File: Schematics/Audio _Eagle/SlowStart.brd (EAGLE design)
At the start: 99.1 x 76.2 mm, 20 parts, among them P1 MOLEX_6P

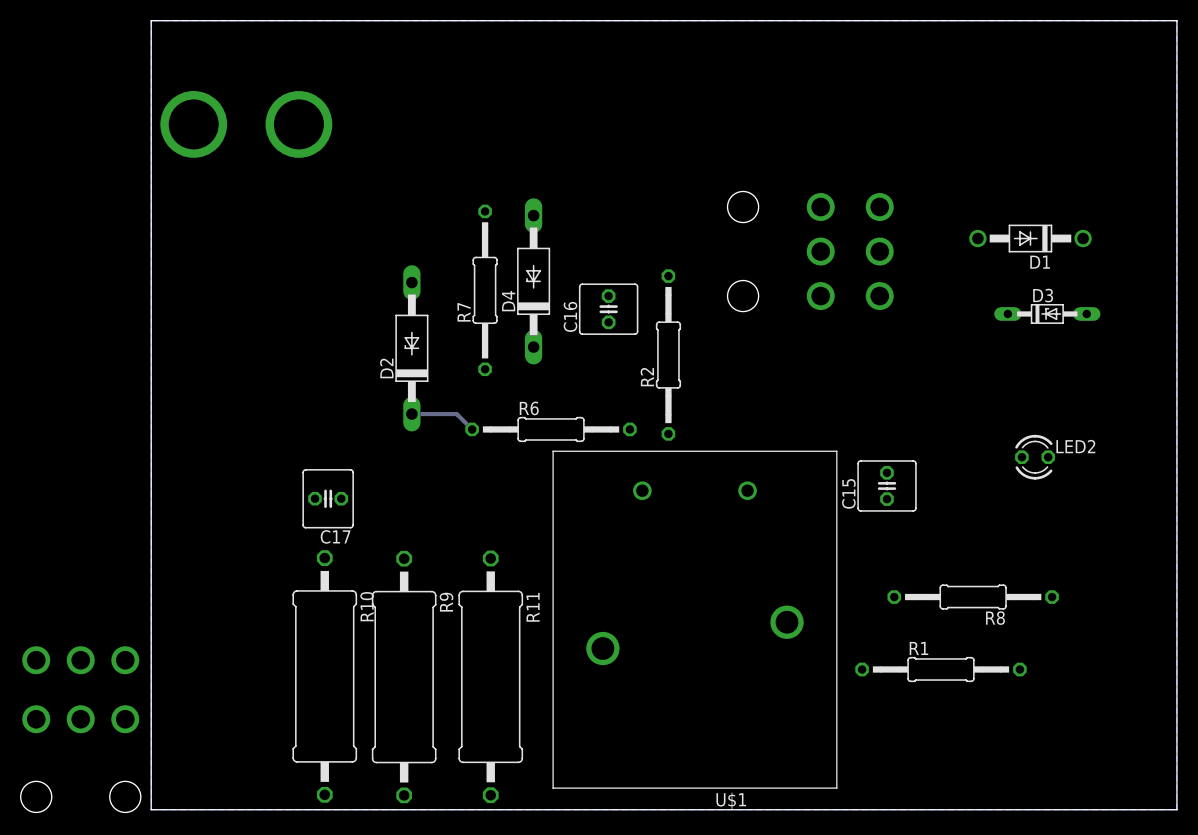
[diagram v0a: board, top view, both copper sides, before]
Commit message: created screw terminal and added data sheet
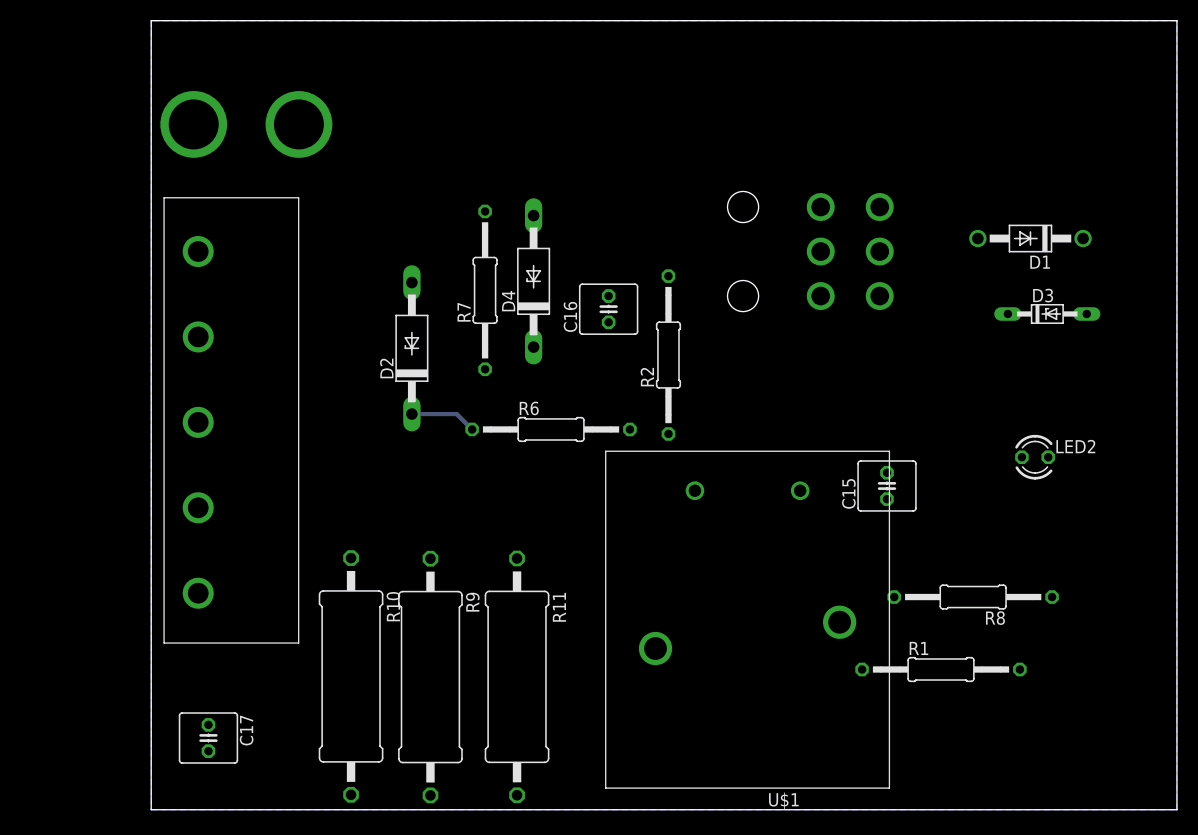
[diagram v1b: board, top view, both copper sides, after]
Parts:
- removed P1: MOLEX_6P, Amplifier_Parts:MOLEX_6P
- added U$2: SCREW_TERMINAL_5, Amplifier_Parts:SCREW_TERMINAL_5
- moved C17 25.8 mm to (5.53, 6.93), turned to 270 degrees
- moved U$1 5.08 mm to (57.6, 23.2)
- moved R10 2.54 mm to (19.3, 12.9)
- moved R11 2.54 mm to (35.3, 12.8)
- moved R9 2.54 mm to (27.0, 12.8)
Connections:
- removed net N$6: P1.P$6, U$4.P$2
- new net N$2: U$2.P$6, U$4.P$2
- net GND: now also U$2.P$5; no longer P1.P$4
- net N$1: now also U$2.P$2; no longer P1.P$1
- net VAC+: now also U$2.P$4; no longer P1.P$3
- net VAC-: now also U$2.P$3; no longer P1.P$2
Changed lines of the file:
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@@
 <element name="R7" library="resistor" package="0207/15" value="390" x="32.2445875" y="50.158621875" rot="R90"/>
 <element name="R8" library="resistor" package="0207/15" value="10k" x="79.379503125" y="20.540834375" rot="R180"/>
-<element name="R9" library="rcl" package="0617/22" value="68" x="24.427478125" y="12.812734375" rot="R270"/>
+<element name="R9" library="rcl" package="0617/22" value="68" x="26.967478125" y="12.812734375" rot="R270"/>
 <element name="C15" library="rcl" package="C025-060X050" value="1uF" x="71.058725" y="31.26728125" rot="R90"/>
 <element name="C16" library="rcl" package="C025-060X050" value="1uF" x="44.175" y="48.33925625" rot="R90"/>
-<element name="C17" library="rcl" package="C025-060X050" value="0.01uF" x="17.0871" y="30.03140625" rot="R180"/>
+<element name="C17" library="rcl" package="C025-060X050" value="0.01uF" x="5.52859375" y="6.9271" rot="R270"/>
 <element name="D1" library="diode" package="DO41-10" value="1N4004" x="84.913978125" y="55.1643875" rot="R180"/>
 <element name="D2" library="diode" package="P1Z12" value="22V" x="25.174603125" y="44.561271875" rot="R90"/>
 <element name="D3" library="diode" package="DO34Z7" value="3.9V" x="86.54215" y="47.877403125"/>
 <element name="D4" library="diode" package="P1Z12" value="28V" x="36.930628125" y="51.028159375" rot="R90"/>
-<element name="R10" library="rcl" package="0617/22" value="68" x="16.760721875" y="12.873171875" rot="R270"/>
-<element name="R11" library="rcl" package="0617/22" value="68" x="32.789928125" y="12.83155" rot="R270"/>
-<element name="U$1" library="Amplifier_Parts" package="RELAY_CM" value="T9AS1D" x="52.512303125" y="23.188921875" rot="R180"/>
+<element name="R10" library="rcl" package="0617/22" value="68" x="19.300721875" y="12.873171875" rot="R270"/>
+<element name="R11" library="rcl" package="0617/22" value="68" x="35.329928125" y="12.83155" rot="R270"/>
+<element name="U$1" library="Amplifier_Parts" package="RELAY_CM" value="T9AS1D" x="57.592303125" y="23.188921875" rot="R180"/>
 <element name="LED2" library="led" package="LED3MM" value="TLLG4400" x="85.359234375" y="34.044678125">
 <attribute name="MF" value="VISHAY SEMICONDUCTOR" x="122.189234375" y="-31.995321875" size="1.778" layer="27" display="off"/>
@@
 <element name="R2" library="resistor" package="0207/15" value="100" x="49.953821875" y="43.912103125" rot="R90"/>
 <element name="U$4" library="Amplifier_Parts" package="FUSE_PADS" value="FUSE" x="9.1866" y="66.183428125" rot="R180"/>
-<element name="P1" library="Amplifier_Parts" package="MOLEX_6P" value="MOLEX_6P" x="-8.9535" y="6.319090625"/>
+<element name="U$2" library="Amplifier_Parts" package="SCREW_TERMINAL_5" value="SCREW_TERMINAL_5" x="2.54" y="38.1" rot="R270"/>
 </elements>
 <signals>
@@
 <contactref element="LED2" pad="K"/>
 <contactref element="R2" pad="1"/>
-<contactref element="P1" pad="P$4"/>
 <polygon width="0.4064" layer="16" isolate="1.27">
 <vertex x="0" y="0"/>
@@
 <vertex x="0" y="76.2"/>
 </polygon>
-<wire x1="36.930628125" y1="57.378159375" x2="-11.1035" y2="14.439090625" width="0" layer="19" extent="1-1"/>
+<contactref element="U$2" pad="P$5"/>
 </signal>
 <signal name="VCC">
@@
 <contactref element="C17" pad="1"/>
 <contactref element="U$1" pad="COM"/>
-<contactref element="P1" pad="P$2"/>
-<wire x1="32.789928125" y1="24.26155" x2="61.402303125" y2="18.108921875" width="0" layer="19" extent="1-1"/>
-<wire x1="24.427478125" y1="24.242734375" x2="32.789928125" y2="24.26155" width="0" layer="19" extent="1-1"/>
-<wire x1="16.760721875" y1="24.303171875" x2="24.427478125" y2="24.242734375" width="0" layer="19" extent="1-1"/>
-<wire x1="18.3571" y1="30.03140625" x2="16.760721875" y2="24.303171875" width="0" layer="19" extent="1-1"/>
-<wire x1="-11.1035" y1="8.739090625" x2="16.760721875" y2="24.303171875" width="0" layer="19" extent="1-1"/>
+<contactref element="U$2" pad="P$3"/>
+<wire x1="35.329928125" y1="24.26155" x2="66.482303125" y2="18.108921875" width="0" layer="19" extent="1-1"/>
+<wire x1="26.967478125" y1="24.242734375" x2="35.329928125" y2="24.26155" width="0" layer="19" extent="1-1"/>
+<wire x1="19.300721875" y1="24.303171875" x2="26.967478125" y2="24.242734375" width="0" layer="19" extent="1-1"/>
+<wire x1="4.54" y1="37.41" x2="19.300721875" y2="24.303171875" width="0" layer="19" extent="1-1"/>
+<wire x1="5.52859375" y1="8.1971" x2="19.300721875" y2="24.303171875" width="0" layer="19" extent="1-1"/>
 </signal>
 <signal name="N$8">
@@
 <contactref element="C17" pad="2"/>
 <contactref element="U$1" pad="NO"/>
-<wire x1="43.622303125" y1="15.568921875" x2="70.35879375" y2="58.208578125" width="0" layer="19" extent="1-1"/>
-<wire x1="32.789928125" y1="1.40155" x2="43.622303125" y2="15.568921875" width="0" layer="19" extent="1-1"/>
-<wire x1="24.427478125" y1="1.382734375" x2="32.789928125" y2="1.40155" width="0" layer="19" extent="1-1"/>
-<wire x1="16.760721875" y1="1.443171875" x2="24.427478125" y2="1.382734375" width="0" layer="19" extent="1-1"/>
-<wire x1="15.8171" y1="30.03140625" x2="16.760721875" y2="1.443171875" width="0" layer="19" extent="1-1"/>
+<wire x1="48.702303125" y1="15.568921875" x2="70.35879375" y2="58.208578125" width="0" layer="19" extent="1-1"/>
+<wire x1="35.329928125" y1="1.40155" x2="48.702303125" y2="15.568921875" width="0" layer="19" extent="1-1"/>
+<wire x1="26.967478125" y1="1.382734375" x2="35.329928125" y2="1.40155" width="0" layer="19" extent="1-1"/>
+<wire x1="19.300721875" y1="1.443171875" x2="26.967478125" y2="1.382734375" width="0" layer="19" extent="1-1"/>
+<wire x1="5.52859375" y1="5.6571" x2="19.300721875" y2="1.443171875" width="0" layer="19" extent="1-1"/>
 </signal>
 <signal name="N$10">
@@
 <contactref element="C16" pad="1"/>
 <contactref element="U$1" pad="COIL-"/>
-<wire x1="44.175" y1="47.06925625" x2="89.993978125" y2="55.1643875" width="0" layer="19" extent="1-1"/>
+<wire x1="52.512303125" y1="30.808921875" x2="89.993978125" y2="55.1643875" width="0" layer="19" extent="1-1"/>
+<wire x1="44.175" y1="47.06925625" x2="52.512303125" y2="30.808921875" width="0" layer="19" extent="1-1"/>
 <wire x1="36.930628125" y1="44.678159375" x2="44.175" y2="47.06925625" width="0" layer="19" extent="1-1"/>
 <wire x1="32.2445875" y1="57.778621875" x2="36.930628125" y2="44.678159375" width="0" layer="19" extent="1-1"/>
-<wire x1="47.432303125" y1="30.808921875" x2="44.175" y2="47.06925625" width="0" layer="19" extent="1-1"/>
 </signal>
 <signal name="N$11">
@@
 <signal name="N$1">
 <contactref element="U$4" pad="P$1"/>
-<contactref element="P1" pad="P$1"/>
-<wire x1="-2.5035" y1="8.739090625" x2="14.2666" y2="66.183428125" width="0" layer="19" extent="1-1"/>
-</signal>
-<signal name="N$6">
-<contactref element="U$4" pad="P$2"/>
-<contactref element="P1" pad="P$6"/>
-<wire x1="-2.5035" y1="14.439090625" x2="4.1066" y2="66.183428125" width="0" layer="19" extent="1-1"/>
+<contactref element="U$2" pad="P$2"/>
+<wire x1="4.54" y1="45.66" x2="14.2666" y2="66.183428125" width="0" layer="19" extent="1-1"/>
 </signal>
 <signal name="VAC+">
 <contactref element="U$3" pad="P$3"/>
-<contactref element="P1" pad="P$3"/>
-<wire x1="-6.8035" y1="8.739090625" x2="64.65879375" y2="53.908578125" width="0" layer="19" extent="1-1"/>
+<contactref element="U$2" pad="P$4"/>
+<wire x1="4.54" y1="53.91" x2="64.65879375" y2="53.908578125" width="0" layer="19" extent="1-1"/>
+</signal>
+<signal name="N$2">
+<contactref element="U$4" pad="P$2"/>
+<contactref element="U$2" pad="P$6"/>
+<wire x1="4.54" y1="20.91" x2="4.1066" y2="66.183428125" width="0" layer="19" extent="1-1"/>
 </signal>
 </signals>
